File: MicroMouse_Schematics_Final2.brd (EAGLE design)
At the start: 227 x 80 mm, 64 parts

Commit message: Final Board (motor on top)
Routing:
- net LMTR+: track 79.3 -> 114.8 mm
- net S$1: track 276.3 -> 261.4 mm, vias 19 -> 21
- net LPWM_B: track 157.3 -> 170.5 mm, vias 7 -> 9
- net +3V3: track 324.2 -> 336.9 mm, vias 24 -> 21
- net LENC_B: track 17.2 -> 25.4 mm
- net SWDIO: track 95.2 -> 90.4 mm
- net N$25: track 18.8 -> 20.4 mm
- net +5V: track 251.1 -> 252.6 mm
- net VBAT: track 120.0 -> 119.3 mm

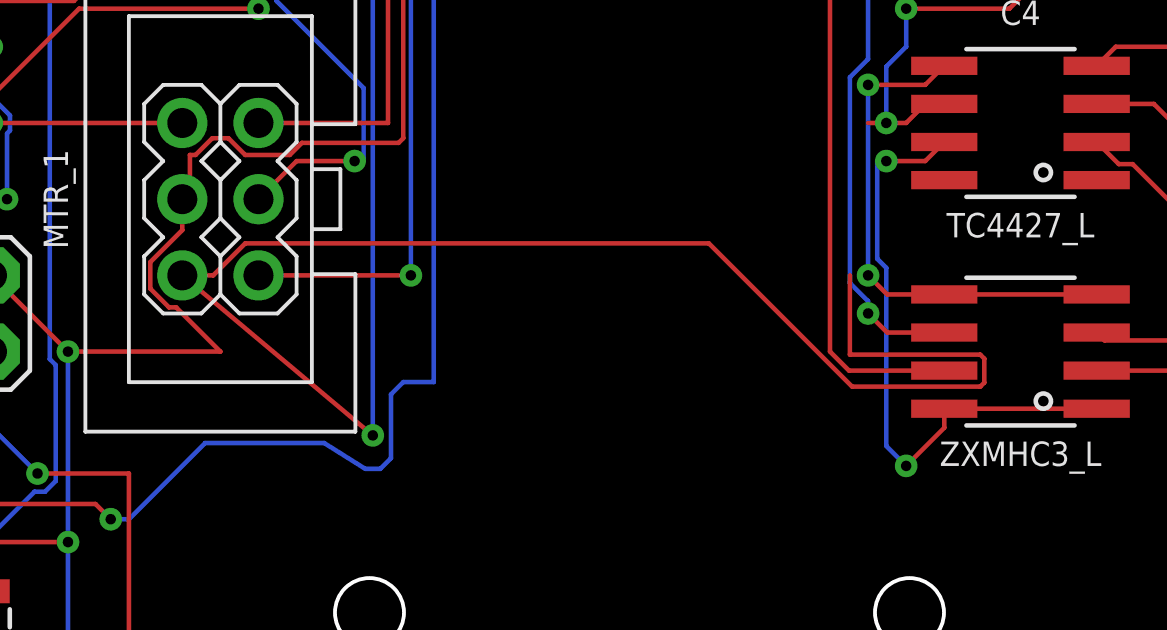
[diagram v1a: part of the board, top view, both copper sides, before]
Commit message: No motor mount bs
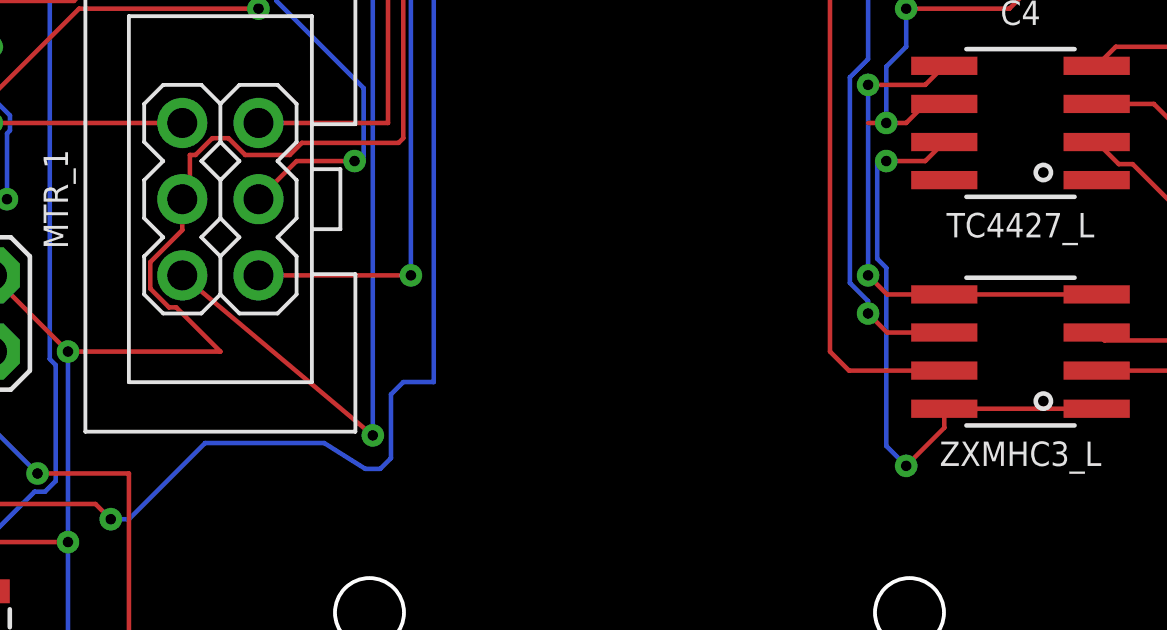
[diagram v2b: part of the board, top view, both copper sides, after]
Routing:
- net LMTR+: track 114.8 -> 77.6 mm
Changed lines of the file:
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@@
 <via x="101.6" y="17.526" extent="1-16" drill="0.35"/>
 <wire x1="101.6" y1="17.526" x2="95.25" y2="22.86" width="0.1524" layer="1"/>
-<wire x1="121.8495875" y1="19.1516" x2="121.9835" y2="19.2855125" width="0.1524" layer="1"/>
-<wire x1="121.9835" y1="19.2855125" x2="121.9835" y2="20.0844875" width="0.1524" layer="1"/>
-<wire x1="121.9835" y1="20.0844875" x2="121.8495875" y2="20.2184" width="0.1524" layer="1"/>
-<wire x1="95.25" y1="22.86" x2="96.2813125" y2="22.86" width="0.1524" layer="1"/>
-<wire x1="96.2813125" y1="22.86" x2="97.3481125" y2="23.9268" width="0.1524" layer="1"/>
-<wire x1="117.5032" y1="20.2184" x2="117.5032" y2="22.86" width="0.1524" layer="1"/>
-<wire x1="121.8495875" y1="20.2184" x2="117.5032" y2="20.2184" width="0.1524" layer="1"/>
-<wire x1="117.57734375" y1="19.1516" x2="121.8495875" y2="19.1516" width="0.1524" layer="1"/>
-<wire x1="97.3481125" y1="23.9268" x2="112.80214375" y2="23.9268" width="0.1524" layer="1"/>
-<wire x1="112.80214375" y1="23.9268" x2="117.57734375" y2="19.1516" width="0.1524" layer="1"/>
 </signal>
 <signal name="N$15">

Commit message: Fixed error
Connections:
- net +3V3: no longer C7.1
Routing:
- net +3V3: track 336.9 -> 336.0 mm
- net GND: track 214.8 -> 214.2 mm
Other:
- board size 227 x 80 mm -> 112.7 x 96.3 mm
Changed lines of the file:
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@@
 <?xml version="1.0" encoding="utf-8"?>
 <!DOCTYPE eagle SYSTEM "eagle.dtd">
-<eagle version="8.6.0">
+<eagle version="8.7.0">
 <drawing>
 <settings>
@@
 <board>
 <plain>
-<wire x1="0" y1="0" x2="227" y2="0" width="0" layer="20"/>
-<wire x1="227" y1="0" x2="227" y2="80" width="0" layer="20"/>
-<wire x1="227" y1="80" x2="0" y2="80" width="0" layer="20"/>
-<wire x1="0" y1="80" x2="0" y2="0" width="0" layer="20"/>
+<wire x1="42.164" y1="-7.62" x2="154.864" y2="-7.112" width="0" layer="20"/>
+<wire x1="154.864" y1="-7.112" x2="154.864" y2="88.636" width="0" layer="20"/>
+<wire x1="154.864" y1="88.636" x2="42.164" y2="88.128" width="0" layer="20"/>
+<wire x1="42.164" y1="88.128" x2="42.164" y2="-7.62" width="0" layer="20"/>
 </plain>
 <attributes>
@@
 <wire x1="132.08" y1="49.53" x2="133.72" y2="49.53" width="0.1524" layer="1"/>
 <wire x1="133.72" y1="49.53" x2="134.62" y2="48.63" width="0.1524" layer="1"/>
-<wire x1="132.08" y1="49.53" x2="132.08" y2="55.88" width="0.1524" layer="16"/>
-<via x="132.08" y="55.88" extent="1-16" drill="0.35"/>
-<wire x1="130.81" y1="55.88" x2="132.08" y2="55.88" width="0.1524" layer="16"/>
-<wire x1="132.08" y1="55.88" x2="132.98" y2="54.98" width="0.1524" layer="1"/>
+<wire x1="132.08" y1="49.53" x2="132.08" y2="54.102" width="0.1524" layer="16"/>
+<via x="132.588" y="55.372" extent="1-16" drill="0.35"/>
+<wire x1="132.08" y1="54.102" x2="132.588" y2="55.372" width="0.1524" layer="16"/>
+<wire x1="132.588" y1="55.372" x2="132.98" y2="54.98" width="0.1524" layer="1"/>
 <wire x1="132.98" y1="54.98" x2="137.16" y2="54.98" width="0.1524" layer="1"/>
 <wire x1="126.4666" y1="55.7784" x2="126.9295875" y2="55.7784" width="0.1524" layer="1"/>
@@
 <wire x1="94.488" y1="37.084" x2="94.9876" y2="36.5844" width="0.1524" layer="1"/>
 <wire x1="94.9876" y1="36.5844" x2="97.79" y2="36.5844" width="0.1524" layer="1"/>
-<wire x1="130.81" y1="55.88" x2="130.81" y2="55.51" width="0" layer="19" extent="1-16"/>
+<wire x1="130.81" y1="55.51" x2="132.45" y2="55.51" width="0.1524" layer="1"/>
+<wire x1="132.45" y1="55.51" x2="132.588" y2="55.372" width="0.1524" layer="1"/>
 </signal>
 <signal name="+5V">
@@
 <contactref element="STM32F401" pad="VBAT"/>
 <contactref element="C6" pad="1"/>
-<contactref element="C7" pad="1"/>
 <contactref element="STM32F401" pad="VDDA"/>
 <contactref element="STM32F401" pad="VDD_2"/>
@@
 <wire x1="78.74" y1="26.67" x2="78.37" y2="27.04" width="0.1524" layer="1"/>
 <wire x1="78.37" y1="27.04" x2="76.2" y2="27.04" width="0.1524" layer="1"/>
-<wire x1="88.9" y1="22.86" x2="84.72" y2="27.04" width="0.1524" layer="1"/>
-<wire x1="84.72" y1="27.04" x2="85.736" y2="27.94" width="0.1524" layer="1"/>
+<wire x1="88.9" y1="22.86" x2="85.736" y2="26.532" width="0.1524" layer="1"/>
+<wire x1="85.736" y1="26.532" x2="85.995565625" y2="27.26993125" width="0.1524" layer="1"/>
 <via x="85.736" y="27.94" extent="1-16" drill="0.35"/>
+<wire x1="85.995565625" y1="27.26993125" x2="85.736" y2="27.94" width="0.1524" layer="1"/>
 <wire x1="78.74" y1="54.99" x2="69.47" y2="54.99" width="0.1524" layer="1"/>
 <wire x1="69.47" y1="54.99" x2="67.31" y2="57.15" width="0.1524" layer="1"/>
@@
 <wire x1="145.49" y1="48.26" x2="145.49" y2="54.304" width="0.1524" layer="1"/>
 <wire x1="145.49" y1="54.304" x2="145.796" y2="54.61" width="0.1524" layer="1"/>
-<wire x1="84.7607125" y1="27.9807125" x2="84.72" y2="27.94" width="0" layer="19" extent="1-1"/>
 </signal>
 <signal name="N$4">
@@
 <wire x1="81.07" y1="46.526" x2="81.07" y2="45.12" width="0.1524" layer="1"/>
 <wire x1="63.1433125" y1="45.2786" x2="63.0094" y2="45.1446875" width="0.1524" layer="1"/>
-<wire x1="71.34445" y1="45.2786" x2="64.008" y2="45.2786" width="0.1524" layer="1"/>
-<wire x1="64.008" y1="45.2786" x2="63.1433125" y2="45.2786" width="0.1524" layer="1"/>
+<wire x1="71.34445" y1="45.2786" x2="63.1433125" y2="45.2786" width="0.1524" layer="1"/>
 <wire x1="74.92735" y1="46.9336" x2="72.99945" y2="46.9336" width="0.1524" layer="1"/>
 <wire x1="72.99945" y1="46.9336" x2="71.34445" y2="45.2786" width="0.1524" layer="1"/>
@@
 <wire x1="75.08425" y1="42.26185" x2="75.08425" y2="42.38235" width="0.1524" layer="16"/>
 <wire x1="75.08425" y1="42.38235" x2="74.5748" y2="42.8918" width="0.1524" layer="16"/>
-<wire x1="73.0532" y1="35.81665" x2="73.0532" y2="42.164" width="0.1524" layer="16"/>
-<wire x1="73.0532" y1="42.164" x2="73.0532" y2="42.93695" width="0.1524" layer="16"/>
+<wire x1="73.0532" y1="35.81665" x2="73.0532" y2="42.93695" width="0.1524" layer="16"/>
 <wire x1="73.0532" y1="42.93695" x2="73.3612" y2="43.24495" width="0.1524" layer="16"/>
 <wire x1="73.3612" y1="43.24495" x2="73.3612" y2="52.76875" width="0.1524" layer="16"/>
 <wire x1="73.3612" y1="52.76875" x2="74.53925" y2="53.9468" width="0.1524" layer="16"/>
 <wire x1="75.04195" y1="53.9468" x2="76.2988" y2="52.68995" width="0.1524" layer="16"/>
-<wire x1="76.2988" y1="52.68995" x2="76.2988" y2="43.18" width="0.1524" layer="16"/>
-<wire x1="76.2988" y1="43.18" x2="76.2988" y2="42.2628" width="0.1524" layer="16"/>
+<wire x1="76.2988" y1="52.68995" x2="76.2988" y2="42.2628" width="0.1524" layer="16"/>
 </signal>
 <signal name="NRST">
@@
 <wire x1="74.6932" y1="30.4628" x2="75.94335" y2="30.4628" width="0.1524" layer="16"/>
 <wire x1="75.94335" y1="30.4628" x2="76.4032" y2="30.00295" width="0.1524" layer="16"/>
-<wire x1="76.4032" y1="30.00295" x2="76.4032" y2="25.4" width="0.1524" layer="16"/>
-<wire x1="76.4032" y1="25.4" x2="76.4032" y2="23.41335" width="0.1524" layer="16"/>
+<wire x1="76.4032" y1="30.00295" x2="76.4032" y2="23.41335" width="0.1524" layer="16"/>
 <wire x1="78.0768" y1="33.02" x2="77.681303125" y2="33.415496875" width="0.1524" layer="16"/>
 <wire x1="77.681303125" y1="33.415496875" x2="77.681303125" y2="33.5707" width="0.1524" layer="16"/>
@@
 <wire x1="79.547425" y1="34.690875" x2="78.801478125" y2="34.690875" width="0.1524" layer="1"/>
 <wire x1="78.801478125" y1="34.690875" x2="77.625203125" y2="33.5146" width="0.1524" layer="1"/>
-<wire x1="78.07" y1="38.62" x2="75.184" y2="38.62" width="0.1524" layer="1"/>
-<wire x1="75.184" y1="38.62" x2="74.688" y2="38.62" width="0.1524" layer="1"/>
+<wire x1="78.07" y1="38.62" x2="74.688" y2="38.62" width="0.1524" layer="1"/>
 <wire x1="74.688" y1="38.62" x2="74.676" y2="38.608" width="0.1524" layer="1"/>
 <wire x1="74.688" y1="38.62" x2="74.688" y2="36.63344375" width="0.1524" layer="1"/>
@@
 <wire x1="95.25" y1="55.88" x2="96.52" y2="57.15" width="0.1524" layer="1"/>
 <wire x1="96.52" y1="57.15" x2="101.6" y2="57.15" width="0.1524" layer="1"/>
-<wire x1="101.6" y1="57.15" x2="101.6" y2="57.912" width="0.1524" layer="1"/>
-<wire x1="101.6" y1="57.912" x2="101.6" y2="58.42" width="0.1524" layer="1"/>
 <wire x1="78.07" y1="42.62" x2="76.252" y2="42.62" width="0.1524" layer="1"/>
 <wire x1="76.252" y1="42.62" x2="76.2" y2="42.672" width="0.1524" layer="1"/>
@@
 <wire x1="73.66" y1="59.944" x2="75.184" y2="61.468" width="0.1524" layer="1"/>
 <wire x1="75.184" y1="61.468" x2="101.6" y2="61.468" width="0.1524" layer="1"/>
-<wire x1="101.6" y1="61.468" x2="101.6" y2="58.42" width="0.1524" layer="1"/>
+<wire x1="101.6" y1="61.468" x2="101.6" y2="57.15" width="0.1524" layer="1"/>
 </signal>
 <signal name="RMTR-">
@@
 <wire x1="66.04" y1="36.068" x2="66.04" y2="37.3332875" width="0.1524" layer="1"/>
 <wire x1="66.04" y1="37.3332875" x2="66.1999125" y2="37.4932" width="0.1524" layer="1"/>
-<wire x1="66.1999125" y1="37.4932" x2="67.05" y2="37.4932" width="0.1524" layer="1"/>
-<wire x1="67.05" y1="37.4932" x2="67.05" y2="37.745" width="0" layer="19" extent="1-1"/>
+<wire x1="66.1999125" y1="37.4932" x2="66.548" y2="37.592" width="0.1524" layer="1"/>
+<wire x1="66.548" y1="37.592" x2="67.056" y2="37.739" width="0.1524" layer="1"/>
+<wire x1="67.056" y1="37.739" x2="67.05" y2="37.745" width="0.1524" layer="1"/>
 </signal>
 <signal name="N$11">
@@
 <contactref element="ULN2003A" pad="4C"/>
 <contactref element="R4" pad="1"/>
-<wire x1="91.44" y1="75.3" x2="88.08" y2="71.94" width="0.1524" layer="1"/>
-<wire x1="88.08" y1="71.94" x2="87.768" y2="71.628" width="0.1524" layer="1"/>
+<wire x1="91.44" y1="75.3" x2="87.768" y2="71.628" width="0.1524" layer="1"/>
 <wire x1="87.768" y1="71.628" x2="70.104" y2="71.628" width="0.1524" layer="1"/>
 <wire x1="70.104" y1="71.628" x2="70.11743125" y2="71.61456875" width="0.1524" layer="1"/>
@@
 <wire x1="88.53" y1="12.7" x2="85.09" y2="12.7" width="0.1524" layer="1"/>
 <wire x1="85.09" y1="12.7" x2="82.55" y2="15.24" width="0.1524" layer="16"/>
-<wire x1="82.55" y1="15.24" x2="82.55" y2="24.892" width="0.1524" layer="16"/>
-<wire x1="82.55" y1="24.892" x2="82.55" y2="25.4" width="0.1524" layer="16"/>
+<wire x1="82.55" y1="15.24" x2="82.55" y2="26.722953125" width="0.1524" layer="16"/>
 <wire x1="84.46193125" y1="32.02261875" x2="84.46193125" y2="31.51991875" width="0.1524" layer="1"/>
 <wire x1="85.07" y1="33.62" x2="85.07" y2="32.6306875" width="0.1524" layer="1"/>
@@
 <via x="80.8792" y="29.0706" extent="1-16" drill="0.35"/>
 <wire x1="80.8792" y1="29.0706" x2="81.1812" y2="28.7686" width="0.1524" layer="16"/>
-<wire x1="82.55" y1="26.722953125" x2="82.55" y2="25.4" width="0.1524" layer="16"/>
 <wire x1="81.1812" y1="28.7686" x2="81.1812" y2="28.091753125" width="0.1524" layer="16"/>
 <wire x1="81.1812" y1="28.091753125" x2="82.55" y2="26.722953125" width="0.1524" layer="16"/>
@@
 <wire x1="70.104" y1="30.988" x2="70.104" y2="53.086" width="0.1524" layer="16"/>
 <wire x1="70.104" y1="53.086" x2="69.85" y2="53.34" width="0.1524" layer="16"/>
-<wire x1="81.6966625" y1="30.7676" x2="73.152" y2="30.7676" width="0.1524" layer="1"/>
-<wire x1="73.152" y1="30.7676" x2="71.8484" y2="30.7676" width="0.1524" layer="1"/>
+<wire x1="81.6966625" y1="30.7676" x2="71.8484" y2="30.7676" width="0.1524" layer="1"/>
 </signal>
 <signal name="RE_RF">

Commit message: Bottoms up
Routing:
- net RE_LF: track 31.2 -> 43.6 mm, vias 1 -> 2
- net +3V3: track 336.0 -> 348.2 mm, vias 21 -> 23
- net N$7: track 53.5 -> 62.5 mm, vias 4 -> 2
- net S$1: track 261.4 -> 269.8 mm
- net LMTR+: track 77.6 -> 69.8 mm, vias 4 -> 3
- net N$18: track 4.25 -> 10.2 mm, vias 0 -> 1
- net RENC_B: track 80.6 -> 84.8 mm, vias 4 -> 5
- net B1: track 66.4 -> 70.2 mm
- net N$3: track 42.7 -> 46.3 mm, vias 4 -> 2
- net N$16: track 8.18 -> 11.5 mm, vias 0 -> 1
- net SWDIO: track 90.4 -> 93.7 mm, vias 9 -> 10
- net RENC_A: track 62.9 -> 65.9 mm, vias 4 -> 5
- net RMTR+: track 53.1 -> 50.7 mm, vias 4 -> 3
- net +5V: track 252.6 -> 254.8 mm, vias 9 -> 12
- net GND: track 214.2 -> 212.2 mm, vias 15 -> 14
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
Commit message: Bottoms
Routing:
- net N$32: track 72.7 -> 75.8 mm
- net +5V: track 254.8 -> 256.8 mm
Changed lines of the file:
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@@
 <wire x1="85.074" y1="3.683" x2="82.423" y2="3.683" width="0.1524" layer="16"/>
 <wire x1="82.423" y1="3.683" x2="82.296" y2="3.556" width="0.1524" layer="16"/>
-<wire x1="60.833" y1="53.356" x2="59.5508" y2="53.356" width="0.1524" layer="16"/>
-<wire x1="59.5508" y1="53.356" x2="59.5348" y2="53.34" width="0.1524" layer="16"/>
-<via x="59.5348" y="53.34" extent="1-16" drill="0.35"/>
-<wire x1="59.5348" y1="53.34" x2="59.5348" y2="60.387684375" width="0.1524" layer="1"/>
-<wire x1="59.5348" y1="60.387684375" x2="61.39443125" y2="63.0435125" width="0.1524" layer="1"/>
+<wire x1="59.699640625" y1="60.623103125" x2="61.39443125" y2="63.0435125" width="0.1524" layer="1"/>
+<wire x1="60.833" y1="53.356" x2="57.928" y2="53.356" width="0.1524" layer="16"/>
+<wire x1="57.928" y1="53.356" x2="57.912" y2="53.34" width="0.1524" layer="16"/>
+<via x="57.912" y="53.34" extent="1-16" drill="0.35"/>
+<wire x1="57.912" y1="53.34" x2="57.912" y2="56.78949375" width="0.1524" layer="1"/>
+<wire x1="57.912" y1="56.78949375" x2="59.699640625" y2="60.623103125" width="0.1524" layer="1"/>
 </signal>
 <signal name="S$3">
@@
 <via x="91.44" y="20.32" extent="1-16" drill="0.35"/>
 <wire x1="91.44" y1="20.32" x2="91.44" y2="13.97" width="0.1524" layer="16"/>
-<wire x1="91.44" y1="13.97" x2="91.44" y2="9.652" width="0.1524" layer="16"/>
+<wire x1="91.44" y1="13.97" x2="91.44" y2="9.144" width="0.1524" layer="16"/>
 <via x="91.44" y="13.97" extent="1-16" drill="0.35"/>
+<wire x1="91.44" y1="9.144" x2="91.44" y2="8.128" width="0.1524" layer="16"/>
 <wire x1="91.44" y1="13.97" x2="78.74" y2="13.97" width="0.1524" layer="1"/>
 <wire x1="78.74" y1="13.97" x2="77.84" y2="13.97" width="0.1524" layer="1"/>
@@
 <wire x1="71.559" y1="22.44085" x2="71.559" y2="20.251" width="0.1524" layer="1"/>
 <wire x1="72.7428" y1="23.62465" x2="71.559" y2="22.44085" width="0.1524" layer="1"/>
-<wire x1="91.186" y1="9.906" x2="91.44" y2="9.652" width="0.1524" layer="16"/>
-<wire x1="91.44" y1="9.652" x2="91.44" y2="8.128" width="0.1524" layer="16"/>
 <wire x1="91.44" y1="8.128" x2="84.836" y2="8.128" width="0.1524" layer="16"/>
 <wire x1="84.836" y1="8.128" x2="85.09" y2="8.382" width="0.1524" layer="16"/>
@@
 <wire x1="97.276596875" y1="35.808596875" x2="96.8784" y2="36.20679375" width="0.1524" layer="16"/>
 <wire x1="96.8784" y1="37.43975" x2="96.8784" y2="36.20679375" width="0.1524" layer="16"/>
-<wire x1="93.472" y1="14.732" x2="96.012" y2="17.272" width="0.1524" layer="16"/>
+<wire x1="93.472" y1="14.732" x2="95.25" y2="16.51" width="0.1524" layer="16"/>
+<wire x1="95.25" y1="16.51" x2="96.012" y2="17.272" width="0.1524" layer="16"/>
 <wire x1="93.472" y1="14.732" x2="92.8652" y2="14.732" width="0.1524" layer="16"/>
 <via x="92.8652" y="14.732" extent="1-16" drill="0.35"/>
@@
 <wire x1="58.928" y1="35.052" x2="58.928" y2="34.8968" width="0.1524" layer="1"/>
 <via x="58.928" y="34.8968" extent="1-16" drill="0.35"/>
-<wire x1="58.928" y1="34.8968" x2="58.928" y2="54.6378875" width="0.1524" layer="16"/>
-<wire x1="58.928" y1="54.6378875" x2="64.008" y2="65.532" width="0.1524" layer="16"/>
+<wire x1="58.928" y1="47.244" x2="58.928" y2="34.8968" width="0.1524" layer="16"/>
 <via x="64.008" y="65.532" extent="1-16" drill="0.35"/>
+<wire x1="64.008" y1="65.532" x2="61.414015625" y2="59.969171875" width="0.1524" layer="16"/>
 <wire x1="64.008" y1="65.532" x2="65.024" y2="66.548" width="0.1524" layer="1"/>
 <wire x1="78.07" y1="37.62" x2="77.08615" y2="37.62" width="0.1524" layer="1"/>
 <wire x1="77.08615" y1="37.62" x2="74.92735" y2="35.4612" width="0.1524" layer="1"/>
 <wire x1="74.92735" y1="35.4612" x2="59.3372" y2="35.4612" width="0.1524" layer="1"/>
+<wire x1="61.414015625" y1="59.969171875" x2="59.35684375" y2="57.912" width="0.1524" layer="16"/>
+<wire x1="59.35684375" y1="57.912" x2="58.516028125" y2="57.912" width="0.1524" layer="16"/>
+<wire x1="58.516028125" y1="57.912" x2="58.000834375" y2="57.39680625" width="0.1524" layer="16"/>
+<wire x1="58.000834375" y1="57.39680625" x2="56.388" y2="53.938071875" width="0.1524" layer="16"/>
+<wire x1="56.388" y1="53.938071875" x2="56.388" y2="49.276" width="0.1524" layer="16"/>
+<wire x1="56.388" y1="49.276" x2="56.896" y2="49.276" width="0.1524" layer="16"/>
+<wire x1="56.896" y1="49.276" x2="58.928" y2="47.244" width="0.1524" layer="16"/>
 </signal>
 <signal name="VCAP_2">

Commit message: Final Board
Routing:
- net S$1: track 269.8 -> 270.9 mm
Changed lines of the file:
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@@
 <wire x1="82.55" y1="27.57" x2="82.92" y2="27.94" width="0.1524" layer="1"/>
 <contactref element="R15" pad="2"/>
-<wire x1="82.55" y1="26.67" x2="82.55" y2="27.57" width="0.1524" layer="1"/>
 <contactref element="C3" pad="C"/>
-<wire x1="83.312" y1="25.908" x2="82.55" y2="26.67" width="0.1524" layer="1"/>
 <wire x1="80.189" y1="50.241" x2="78.74" y2="51.69" width="0.1524" layer="1"/>
 <contactref element="R7" pad="1"/>
 <wire x1="73.66" y1="51.17" x2="78.22" y2="51.17" width="0.1524" layer="1"/>
 <wire x1="78.22" y1="51.17" x2="78.232" y2="51.182" width="0.1524" layer="1"/>
-<wire x1="82.296" y1="26.67" x2="82.55" y2="26.67" width="0.1524" layer="1"/>
 <wire x1="74.93" y1="24.5" x2="74.93" y2="22.49" width="0.1524" layer="1"/>
 <contactref element="R6" pad="1"/>
@@
 <wire x1="79.11" y1="27.94" x2="80.634" y2="26.416" width="0.1524" layer="1"/>
 <wire x1="80.634" y1="26.416" x2="80.772" y2="26.416" width="0.1524" layer="1"/>
-<wire x1="82.296" y1="26.67" x2="82.042" y2="26.416" width="0.1524" layer="1"/>
-<wire x1="82.042" y1="26.416" x2="80.772" y2="26.416" width="0.1524" layer="1"/>
 <wire x1="80.772" y1="26.416" x2="80.641115625" y2="26.546884375" width="0.1524" layer="16"/>
 <wire x1="80.641115625" y1="26.546884375" x2="80.641115625" y2="27.301115625" width="0.1524" layer="16"/>
@@
 <wire x1="83.312" y1="24.384" x2="83.312" y2="24.892" width="0.1524" layer="16"/>
 <via x="83.312" y="24.892" extent="1-16" drill="0.35"/>
-<wire x1="83.312" y1="24.892" x2="83.312" y2="25.908" width="0.1524" layer="1"/>
 <wire x1="97.79" y1="53.34" x2="104.14" y2="53.34" width="0.1524" layer="16"/>
 <wire x1="102.87" y1="50.292" x2="102.743" y2="50.419" width="0.1524" layer="16"/>
@@
 <wire x1="104.14" y1="53.34" x2="104.14" y2="59.436" width="0.1524" layer="16"/>
 <wire x1="104.14" y1="59.436" x2="102.108" y2="59.436" width="0.1524" layer="16"/>
+<wire x1="83.312" y1="24.892" x2="83.312" y2="27.548" width="0.1524" layer="1"/>
+<wire x1="83.312" y1="27.548" x2="82.92" y2="27.94" width="0.1524" layer="1"/>
+<wire x1="82.92" y1="27.94" x2="81.396" y2="26.416" width="0.1524" layer="1"/>
+<wire x1="81.396" y1="26.416" x2="80.772" y2="26.416" width="0.1524" layer="1"/>
 </signal>
 <signal name="GND">
@@
 <wire x1="57.912" y1="56.78949375" x2="59.699640625" y2="60.623103125" width="0.1524" layer="1"/>
 </signal>
-<signal name="S$3">
-<wire x1="84.7607125" y1="27.9807125" x2="84.837059375" y2="27.978615625" width="0.1524" layer="1"/>
-</signal>
 <signal name="+3V3">

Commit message: Final Fixed Board
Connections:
- net +3V3: now also C7.1
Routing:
- net +5V: track 256.8 -> 270.5 mm
- net S$1: track 270.9 -> 260.8 mm
- net TX: track 70.5 -> 61.4 mm
- net SWDIO: track 93.7 -> 102.3 mm, vias 10 -> 11
- net N$3: track 46.3 -> 38.0 mm
- net RENC_B: track 84.8 -> 81.9 mm
- net RE_LF: track 43.6 -> 40.7 mm
- net LMTR+: track 69.8 -> 72.6 mm
- net N$7: track 62.5 -> 60.2 mm
- net +3V3: track 347.8 -> 345.8 mm, vias 23 -> 22
- net LPWM_B: track 170.5 -> 172.4 mm
- net B1: track 70.2 -> 68.4 mm
- net RX: track 119.6 -> 117.9 mm, vias 5 -> 3
- net SWCLK: track 76.4 -> 78.1 mm
- net B0: track 65.1 -> 63.6 mm, vias 5 -> 4
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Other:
- board size 112.7 x 96.3 mm -> 227 x 80 mm
